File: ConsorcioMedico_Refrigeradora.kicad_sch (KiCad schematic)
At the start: 43 parts, among them J1 BatteryHolder, J37 SWD, J5 USART, U1 STM32F411RETx, U3 LDL1117, U8 LM2594HVM-5.0, U9 HLK-PMx

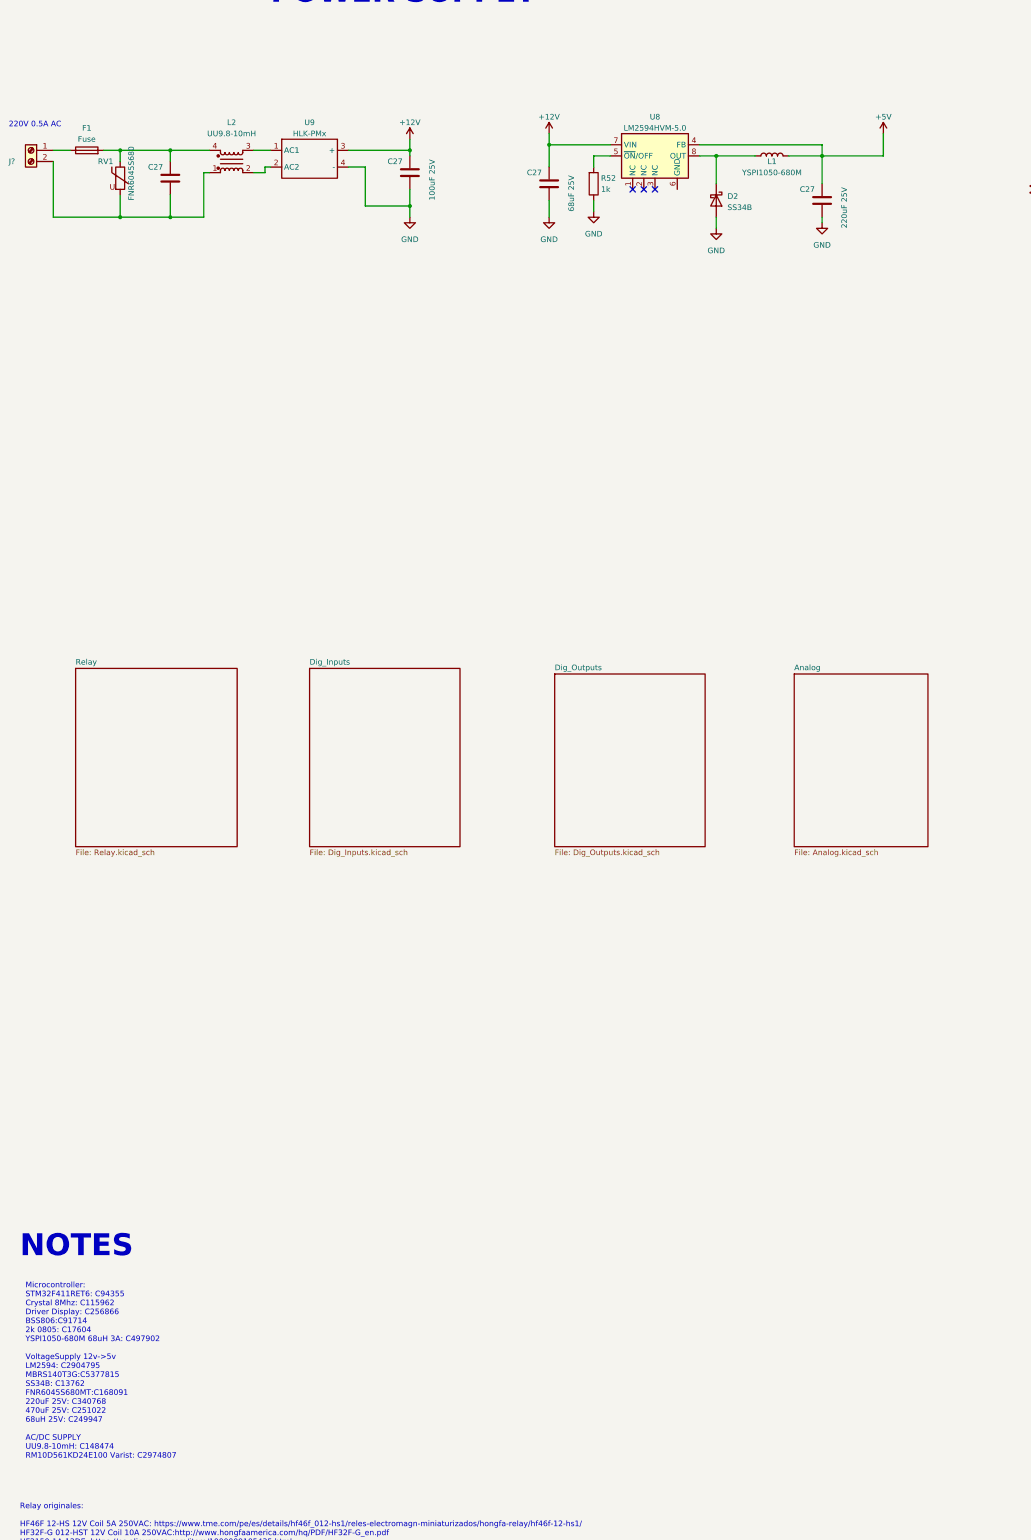
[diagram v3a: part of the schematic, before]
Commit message: SCH: Se cambian la bornera por terminales, se añade un disparo más para el compressor (falta conectarlo al uC), falta modificar, se cambia la fuente switching por otra de menos costo
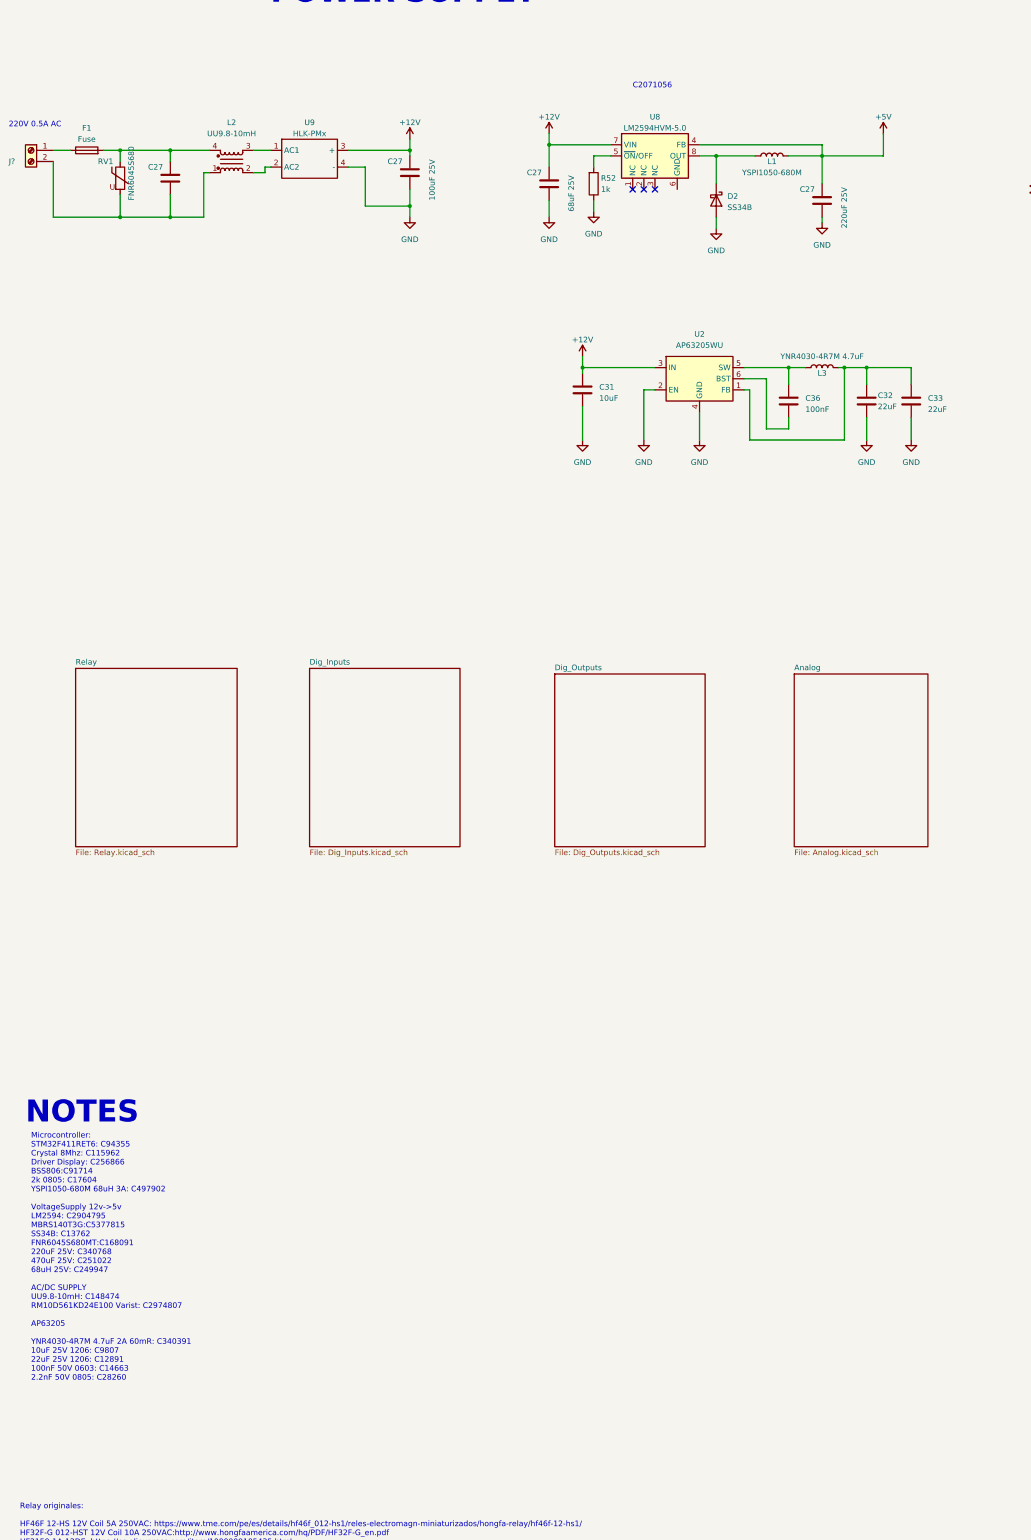
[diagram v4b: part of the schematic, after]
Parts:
- added C31: 10uF, 1-Capacitor:C_1206_3216Metric, symbol 1-Capacitor:C_1206
- added C32, C33: 22uF, 1-Capacitor:C_1206_3216Metric, symbol 1-Capacitor:C_1206
- added C36: 100nF, 1-Capacitor:C_0603_1608Metric, symbol 1-Capacitor:C_0603
- added L3: YNR4030-4R7M 4.7uF, 1-Inductor:Inductor_YNR4030_4x4x3mm_YJYCOIN, symbol Device:L
- added U2: AP63205WU, Package_TO_SOT_SMD:TSOT-23-6, symbol Regulator_Switching:AP63205WU
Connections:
- net +12V: now also C31.1, U2.3 (IN)
- net GND: now also C31.2, C32.2, C33.2, U2.2 (EN), U2.4 (GND)
- new net: C32.1, C33.1, L3.2, U2.1 (FB)
- new net: C36.1, L3.1, U2.5 (SW)
- new net: C36.2, U2.6 (BST)
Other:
- note added: "C2071056"
- note added: "Microcontroller: STM32F411RET6: C94355 Crystal 8Mhz: C115962 Driver Display: C256866 BSS806:C91714 2k 0805: C17604 YSPI1050-680M 68uH 3A: C497902 VoltageSupply 12v->5v LM2594: C2904795 MBRS140T3G:C5377815 SS34B: C13762 FNR6045S680MT:C168091 220uF 25V: C340768 470uF 25V: C251022 68uH 25V: C249947 AC/DC SUPPLY UU9.8-10mH: C148474 RM10D561KD24E100 Varist: C2974807 AP63205 YNR4030-4R7M 4.7uF 2A 60mR: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"
- note removed: "Microcontroller: STM32F411RET6: C94355 Crystal 8Mhz: C115962 Driver Display: C256866 BSS806:C91714 2k 0805: C17604 YSPI1050-680M 68uH 3A: C497902 VoltageSupply 12v->5v LM2594: C2904795 MBRS140T3G:C5377815 SS34B: C13762 FNR6045S680MT:C168091 220uF 25V: C340768 470uF 25V: C251022 68uH 25V: C249947 AC/DC SUPPLY UU9.8-10mH: C148474 RM10D561KD24E100 Varist: C2974807"

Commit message: SCH: Se modificó la posición de algunos pines para mejorar la calidad del ruteado. PCB: Se enruta las señales, quedando la alimentación, pines de programación, relays y planos de gnd
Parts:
- removed C27: 68uF 25V, Capacitor_SMD:CP_Elec_6.3x5.7, symbol Device:C
- removed C27: 220uF 25V, Capacitor_SMD:CP_Elec_6.3x7.7, symbol Device:C
- removed D2: SS34B, 1-Diode:D_SMB, symbol Device:D_Schottky
- removed J?: Screw_Terminal_01x02, 1-Terminal-Block:DG504-5.08-02P_or_SMKDS 2,5-2-5.08, symbol 1-Terminal-Block:DG504-5.08-02P
- removed L1: YSPI1050-680M, Inductor_SMD:L_10.4x10.4_H4.8, symbol Device:L
- removed R52: 1k, 1-Resistor:R_0603_1608Metric, symbol 1-Resistor:R_0603
- removed U8: LM2594HVM-5.0, Package_SO:SOIC-8_3.9x4.9mm_P1.27mm, symbol Regulator_Switching:LM2594HVM-5.0
- added J5, J8: AC, 1-Pad:Solder-Terminal_FS1536_6.3x0.8mm_NINIGI, symbol Connector:Screw_Terminal_01x01
- F1: value Fuse -> 250VAC 0.5AAC
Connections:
- net +5V: now also C32.1, C33.1, L3.2, U2.1 (FB)
- net Button_Buzzer: now also U1.52 (PC11); no longer U1.56 (PB4)
- net Button_Cooling: now also U1.53 (PC12); no longer U1.61 (PB8)
- net Button_Down: now also U1.51 (PC10); no longer U1.59 (PB7)
- net Button_Light: now also U1.54 (PD2); no longer U1.62 (PB9)
- net Button_Touch: now also U1.38 (PC7); no longer U1.57 (PB5)
- net Button_Up: now also U1.39 (PC8); no longer U1.58 (PB6)
- net DIG_IN_0: now also U1.56 (PB4); no longer U1.39 (PC8)
- net DIG_IN_1: now also U1.57 (PB5); no longer U1.38 (PC7)
- net LED_Defrost: now also U1.62 (PB9); no longer U1.34 (PB13)
- net LED_Door: now also U1.61 (PB8); no longer U1.35 (PB14)
- net LED_Status: now also U1.58 (PB6); no longer U1.33 (PB12)
- net LED_TempAlarm: now also U1.59 (PB7); no longer U1.36 (PB15)
- net Relay_Calefac: now also U1.34 (PB13); no longer U1.2 (PC13)
- net Relay_Compressor: now also U1.36 (PB15); no longer U1.53 (PC12)
- net Relay_Fan: now also U1.35 (PB14); no longer U1.51 (PC10)
- net Relay_Light: now also U1.33 (PB12); no longer U1.52 (PC11)
- net at F1.1: now also J8.1 (Pin_1)
- net at C27.2, L2.1, RV1.2: now also J5.1 (Pin_1)
- net Relay_Compressor_Save: now reaches U1.37 (PC6)
- no-connect marks 9 -> 6
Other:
- note added: "DIG"
- note added: "Microcontroller: STM32F411RET6: C94355 Crystal 8Mhz: C115962 Crystal 32.768khz/12.5pF: C32346 Driver Display: C256866 BSS806:C91714 2k 0805: C17604 YSPI1050-680M 68uH 3A: C497902 30pF 0603: C1658 VoltageSupply 12v->5v LM2594: C2904795 MBRS140T3G:C5377815 SS34B: C13762 FNR6045S680MT:C168091 220uF 25V: C340768 470uF 25V: C251022 68uH 25V: C249947 AC/DC SUPPLY UU9.8-10mH: C148474 RM10D561KD24E100 Va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"
- note removed: "C2071056"
- note removed: "INPUTS"
- note removed: "Microcontroller: STM32F411RET6: C94355 Crystal 8Mhz: C115962 Driver Display: C256866 BSS806:C91714 2k 0805: C17604 YSPI1050-680M 68uH 3A: C497902 VoltageSupply 12v->5v LM2594: C2904795 MBRS140T3G:C5377815 SS34B: C13762 FNR6045S680MT:C168091 220uF 25V: C340768 470uF 25V: C251022 68uH 25V: C249947 AC/DC SUPPLY UU9.8-10mH: C148474 RM10D561KD24E100 Varist: C2974807 AP63205 YNR4030-4R7M 4.7uF 2A 60mR: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"
- moved on the sheet: C31, C32, C33, C36, C?, L3, U2, Y?

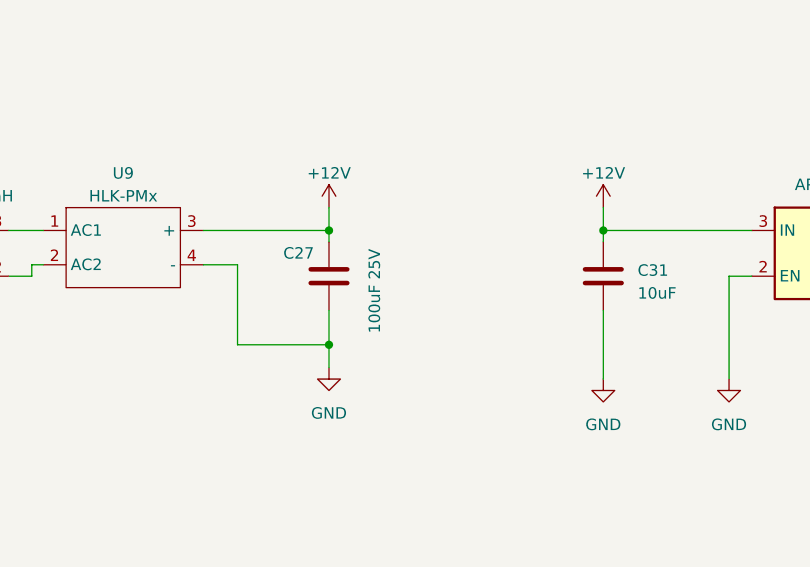
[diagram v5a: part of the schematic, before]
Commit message: SCH: Se añadieron pads en el capacitor de la fuente principal en caso de que el de tipo SMD no dure mucho. PCB: Se enrutó, se colocaron los planos GND, se acomodó la serigrafía
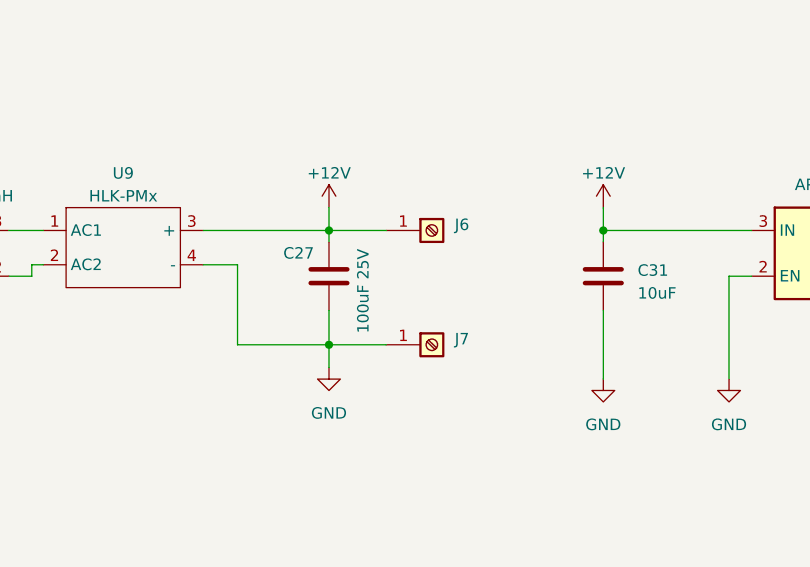
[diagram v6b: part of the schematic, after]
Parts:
- added J6, J7: Screw_Terminal_01x01, 1-Pad:Pad_0.7mm_1.3mm, symbol Connector:Screw_Terminal_01x01
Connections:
- net +12V: now also J6.1 (Pin_1)
- net GND: now also J7.1 (Pin_1)
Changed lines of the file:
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@@
     (stroke (width 0) (type default))
   )
+  (wire (pts (xy 105.41 81.28) (xy 111.76 81.28))
+    (stroke (width 0) (type default))
+  )
   (wire (pts (xy 303.53 124.46) (xy 308.61 124.46))
     (stroke (width 0) (type default))
@@
     (stroke (width 0) (type default))
   )
+  (wire (pts (xy 105.41 68.58) (xy 111.76 68.58))
+    (stroke (width 0) (type default))
+  )
   (wire (pts (xy 414.02 71.12) (xy 412.75 71.12))
     (stroke (width 0) (type default))
@@
     )
   )
+  (symbol (lib_id "Connector:Screw_Terminal_01x01") (at 116.84 68.58 0) (unit 1)
+    (in_bom yes) (on_board yes) (dnp no) (fields_autoplaced)
+    (property "Reference" "J6" (at 119.38 67.945 0)
+      (effects (font (size 1.27 1.27)) (justify left))
+    )
+    (property "Value" "Screw_Terminal_01x01" (at 119.38 70.485 0)
+      (effects (font (size 1.27 1.27)) (justify left) hide)
+    )
+    (property "Footprint" "1-Pad:Pad_0.7mm_1.3mm" (at 116.84 68.58 0)
+      (effects (font (size 1.27 1.27)) hide)
+    )
+    (property "Datasheet" "~" (at 116.84 68.58 0)
+      (effects (font (size 1.27 1.27)) hide)
+    )
+    (pin "1")
+    (instances
+      (project "ConsorcioMedico_Refrigeradora"
+        (path "/e86bbed0-5bdc-4982-8297-fb5cecea731c"
+          (reference "J6") (unit 1)
+        )
+      )
+    )
+  )
   (symbol (lib_id "1-Capacitor:C_1206") (at 210.82 76.2 0) (unit 1)
     (in_bom yes) (on_board yes) (dnp no) (fields_autoplaced)
@@
     )
   )
+  (symbol (lib_id "Connector:Screw_Terminal_01x01") (at 116.84 81.28 0) (unit 1)
+    (in_bom yes) (on_board yes) (dnp no) (fields_autoplaced)
+    (property "Reference" "J7" (at 119.38 80.645 0)
+      (effects (font (size 1.27 1.27)) (justify left))
+    )
+    (property "Value" "Screw_Terminal_01x01" (at 119.38 83.185 0)
+      (effects (font (size 1.27 1.27)) (justify left) hide)
+    )
+    (property "Footprint" "1-Pad:Pad_0.7mm_1.3mm" (at 116.84 81.28 0)
+      (effects (font (size 1.27 1.27)) hide)
+    )
+    (property "Datasheet" "~" (at 116.84 81.28 0)
+      (effects (font (size 1.27 1.27)) hide)
+    )
+    (pin "1")
+    (instances
+      (project "ConsorcioMedico_Refrigeradora"
+        (path "/e86bbed0-5bdc-4982-8297-fb5cecea731c"
+          (reference "J7") (unit 1)
+        )
+      )
+    )
+  )
   (symbol (lib_id "1-Resistor:R_0603") (at 482.6 218.44 180) (unit 1)
     (in_bom yes) (on_board yes) (dnp no)
@@
       (effects (font (size 1.27 1.27)) (justify left))
     )
-    (property "Value" "100uF 25V" (at 110.49 80.01 90)
+    (property "Value" "100uF 25V" (at 109.22 80.01 90)
       (effects (font (size 1.27 1.27)) (justify left))
     )

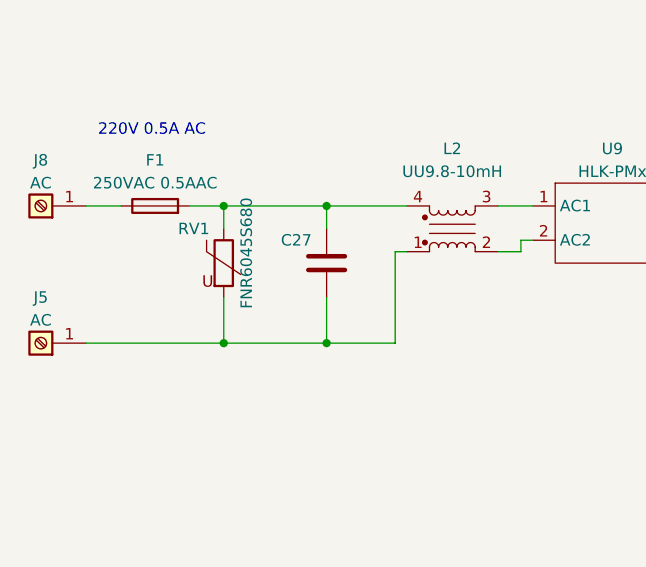
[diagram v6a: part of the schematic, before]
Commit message: SCH: Se modicaron algunos valores y comentarios del sch. PCB: Posiblemente debido a jlcpcb. JLCPCB: Se asigna el código para la soldura
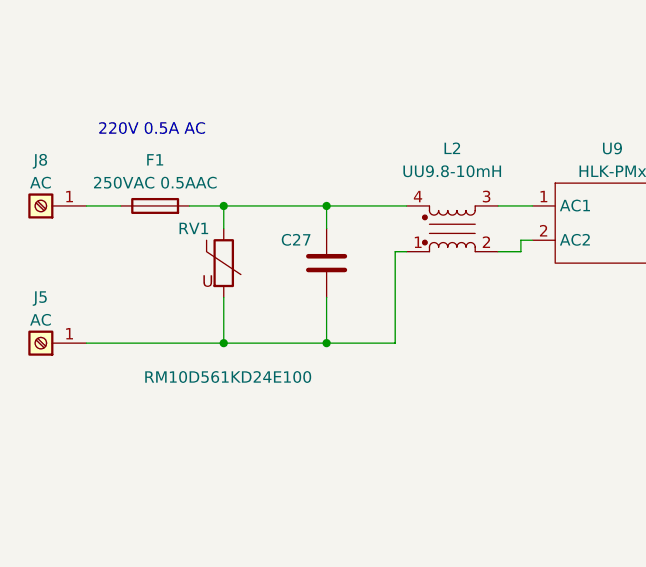
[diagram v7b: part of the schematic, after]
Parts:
- RV1: value FNR6045S680 -> RM10D561KD24E100
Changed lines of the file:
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@@
       (effects (font (size 1.27 1.27)) (justify left))
     )
-    (property "Value" "FNR6045S680" (at 41.91 80.01 90)
+    (property "Value" "RM10D561KD24E100" (at 30.48 87.63 0)
       (effects (font (size 1.27 1.27)) (justify left))
     )
